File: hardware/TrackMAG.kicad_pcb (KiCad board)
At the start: 4 copper layers, 36 x 36 mm, 58 parts, among them J1 USB_C_Socket_USB2.0, J2 Conn_Debug, SW1 SW_RESET, SW2 SW_BOOT, SW3 SW_CALIBRATE, U1 LSM6DS3TR-C, U2 USBLC6-2P6, U3 STM32F103C8T6, U4 LIS2MDL, U5 AMS1117-3.3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

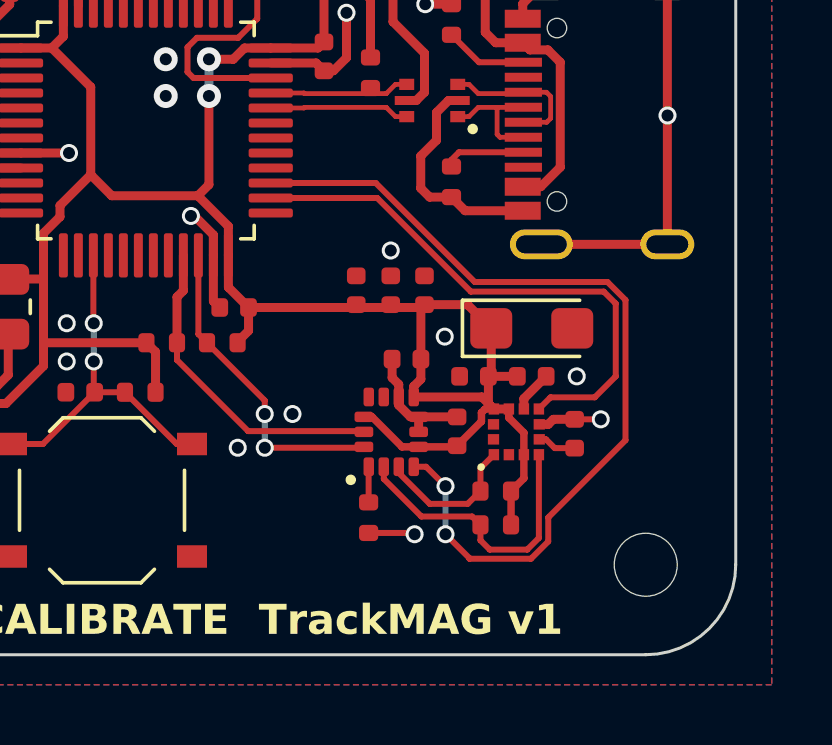
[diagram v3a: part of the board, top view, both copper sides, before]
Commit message: Increase spacing of INT1 line
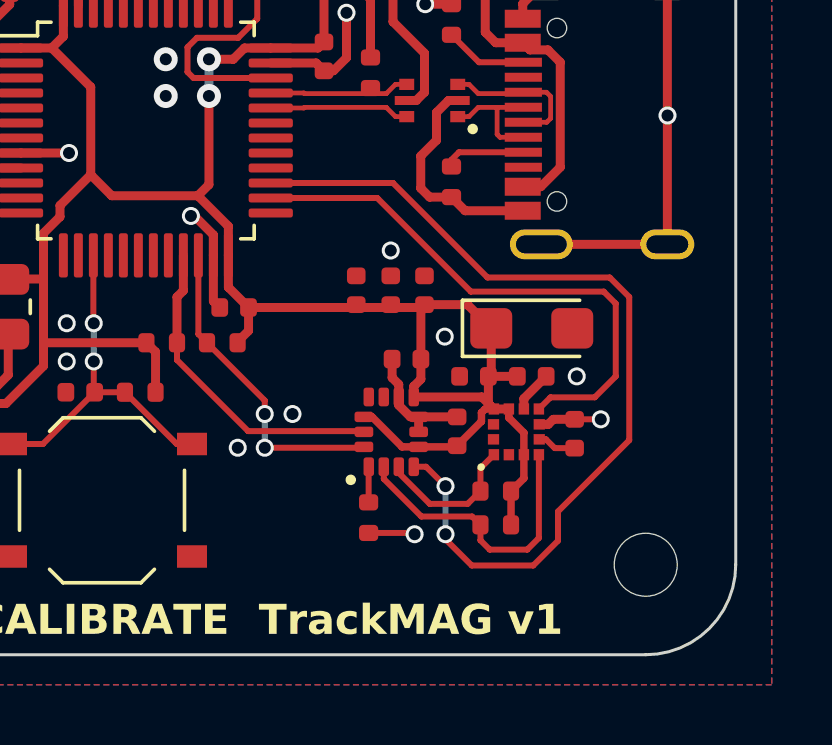
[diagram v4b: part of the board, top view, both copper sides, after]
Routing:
- net INT1: track 29.5 -> 30.2 mm
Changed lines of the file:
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@@
   (segment (start 148.6 103.495) (end 149.85 103.495) (width 0.2) (layer "F.Cu") (net 17))
   (segment (start 148.29 102.67) (end 148.29 103.185) (width 0.2) (layer "F.Cu") (net 17))
-  (segment (start 150.55 103.225) (end 150.55 102.425) (width 0.2) (layer "F.Cu") (net 18))
-  (segment (start 153.125 99.85) (end 153.125 95.175) (width 0.2) (layer "F.Cu") (net 18))
-  (segment (start 147.125 102.9825) (end 147.925 103.7825) (width 0.2) (layer "F.Cu") (net 18))
+  (segment (start 153.25 99.85) (end 153.25 95.075) (width 0.2) (layer "F.Cu") (net 18))
+  (segment (start 150.05 104.025) (end 150.875 103.2) (width 0.2) (layer "F.Cu") (net 18))
   (segment (start 146.477 100.7325) (end 147.125 101.3805) (width 0.2) (layer "F.Cu") (net 18))
-  (segment (start 153.125 95.175) (end 152.525 94.575) (width 0.2) (layer "F.Cu") (net 18))
-  (segment (start 144.8 91.275) (end 144.375 91.275) (width 0.2) (layer "F.Cu") (net 18))
-  (segment (start 141.3 91.275) (end 144.375 91.275) (width 0.2) (layer "F.Cu") (net 18))
-  (segment (start 147.925 103.8) (end 149.975 103.8) (width 0.2) (layer "F.Cu") (net 18))
-  (segment (start 147.925 103.7825) (end 147.925 103.8) (width 0.2) (layer "F.Cu") (net 18))
-  (segment (start 149.975 103.8) (end 150.55 103.225) (width 0.2) (layer "F.Cu") (net 18))
-  (segment (start 150.55 102.425) (end 153.125 99.85) (width 0.2) (layer "F.Cu") (net 18))
-  (segment (start 148.1 94.575) (end 144.8 91.275) (width 0.2) (layer "F.Cu") (net 18))
+  (segment (start 148 104.025) (end 150.05 104.025) (width 0.2) (layer "F.Cu") (net 18))
+  (segment (start 153.25 95.075) (end 152.6 94.425) (width 0.2) (layer "F.Cu") (net 18))
+  (segment (start 147.125 102.9825) (end 147.125 103.15) (width 0.2) (layer "F.Cu") (net 18))
+  (segment (start 148.525 94.425) (end 145.375 91.275) (width 0.2) (layer "F.Cu") (net 18))
+  (segment (start 152.6 94.425) (end 148.525 94.425) (width 0.2) (layer "F.Cu") (net 18))
+  (segment (start 145.375 91.275) (end 141.3 91.275) (width 0.2) (layer "F.Cu") (net 18))
+  (segment (start 147.125 103.15) (end 148 104.025) (width 0.2) (layer "F.Cu") (net 18))
   (segment (start 146.0675 100.7325) (end 146.477 100.7325) (width 0.2) (layer "F.Cu") (net 18))
-  (segment (start 152.525 94.575) (end 148.1 94.575) (width 0.2) (layer "F.Cu") (net 18))
+  (segment (start 150.875 103.2) (end 150.875 102.225) (width 0.2) (layer "F.Cu") (net 18))
   (segment (start 146.0675 100.7325) (end 146.0675 100.7375) (width 0.2) (layer "F.Cu") (net 18))
+  (segment (start 150.875 102.225) (end 153.25 99.85) (width 0.2) (layer "F.Cu") (net 18))
   (via (at 147.125 101.3805) (size 0.6) (drill 0.4) (layers "F.Cu" "B.Cu") (net 18))
   (via (at 147.125 102.9825) (size 0.6) (drill 0.4) (layers "F.Cu" "B.Cu") (net 18))

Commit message: Cleanup
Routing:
- net GND: track 72.8 -> 37.1 mm
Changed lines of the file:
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@@
   (segment (start 146.3 90.375) (end 146.3 91.45) (width 0.3) (layer "F.Cu") (net 2))
   (segment (start 130.1 90.125) (end 129.9 90.325) (width 0.3) (layer "F.Cu") (net 2))
-  (segment (start 154.52 84.68) (end 154.52 82.955) (width 0.3) (layer "F.Cu") (net 2))
-  (segment (start 127.2 87.6) (end 126.175 87.6) (width 0.2) (layer "F.Cu") (net 2))
   (segment (start 134.8875 85.3625) (end 134.8875 83.7875) (width 0.3) (layer "F.Cu") (net 2))
-  (segment (start 132.12 85.795) (end 131.175 85.795) (width 0.3) (layer "F.Cu") (net 2))
   (segment (start 150.25 99.32) (end 150.55 99.32) (width 0.3) (layer "F.Cu") (net 2))
   (segment (start 146.3 91.45) (end 146.595 91.745) (width 0.3) (layer "F.Cu") (net 2))
-  (segment (start 154.52 84.68) (end 154.52 89.02) (width 0.3) (layer "F.Cu") (net 2))
-  (segment (start 149.7 85.8) (end 149.7 85.3) (width 0.3) (layer "F.Cu") (net 2))
   (segment (start 141.3 87.275) (end 142.815 87.275) (width 0.3) (layer "F.Cu") (net 2))
-  (segment (start 150.32 93.32) (end 154.52 93.32) (width 0.3) (layer "F.Cu") (net 2))
-  (segment (start 122.69 90.375) (end 123.9 90.375) (width 0.3) (layer "F.Cu") (net 2))
   (segment (start 149.7375 98.4625) (end 149.7375 98.8075) (width 0.3) (layer "F.Cu") (net 2))
   (segment (start 139.3875 93.004523) (end 138.756292 92.373315) (width 0.3) (layer "F.Cu") (net 2))
@@
   (segment (start 125.59 88.165) (end 125.6 88.175) (width 0.2) (layer "F.Cu") (net 2))
   (segment (start 131.1 91.73) (end 130.435 91.73) (width 0.3) (layer "F.Cu") (net 2))
-  (segment (start 150.32 84.68) (end 154.52 84.68) (width 0.3) (layer "F.Cu") (net 2))
-  (segment (start 125.6 86.875) (end 125.625 86.85) (width 0.2) (layer "F.Cu") (net 2))
-  (segment (start 132.125 85.8) (end 132.12 85.795) (width 0.3) (layer "F.Cu") (net 2))
   (segment (start 129.905 90.33) (end 129.905 91.2) (width 0.3) (layer "F.Cu") (net 2))
   (segment (start 151.2625 99.32) (end 151.43 99.1525) (width 0.2) (layer "F.Cu") (net 2))
-  (segment (start 152.3 99.1525) (end 151.43 99.1525) (width 0.2) (layer "F.Cu") (net 2))
   (segment (start 146.23 99.07) (end 147.51 99.07) (width 0.3) (layer "F.Cu") (net 2))
   (segment (start 139.3875 93.6875) (end 139.3875 95.2125) (width 0.3) (layer "F.Cu") (net 2))
@@
   (segment (start 150.55 99.32) (end 150.7175 99.1525) (width 0.3) (layer "F.Cu") (net 2))
   (segment (start 150.48 97.72) (end 149.7375 98.4625) (width 0.3) (layer "F.Cu") (net 2))
-  (segment (start 149.25 81.84) (end 150.565 81.84) (width 0.3) (layer "F.Cu") (net 2))
-  (segment (start 149.7 92.2) (end 147.78 92.2) (width 0.3) (layer "F.Cu") (net 2))
   (segment (start 143.825 87.1) (end 143.825 85.6) (width 0.3) (layer "F.Cu") (net 2))
-  (segment (start 146.45 85.315) (end 147.325 85.315) (width 0.3) (layer "F.Cu") (net 2))
   (segment (start 129.9 90.325) (end 129.905 90.33) (width 0.3) (layer "F.Cu") (net 2))
-  (segment (start 125.6 88.175) (end 125.6 86.875) (width 0.3) (layer "F.Cu") (net 2))
   (segment (start 154.52 89.03) (end 154.525 89.025) (width 0.3) (layer "F.Cu") (net 2))
   (segment (start 139.3875 93.6875) (end 139.3875 93.004523) (width 0.3) (layer "F.Cu") (net 2))
-  (segment (start 132.6 84.96) (end 132.6 85.325) (width 0.3) (layer "F.Cu") (net 2))
   (segment (start 139.3875 95.2125) (end 139.6 95.425) (width 0.3) (layer "F.Cu") (net 2))
-  (segment (start 144.5625 102.94) (end 146.0525 102.94) (width 0.2) (layer "F.Cu") (net 2))
-  (segment (start 149.7 85.3) (end 150.32 84.68) (width 0.3) (layer "F.Cu") (net 2))
   (segment (start 154 78.2) (end 153.75 78.45) (width 0.3) (layer "F.Cu") (net 2))
   (segment (start 132.975 90.275) (end 131.5 90.275) (width 0.3) (layer "F.Cu") (net 2))
   (segment (start 146.3 90.375) (end 146.825 89.85) (width 0.3) (layer "F.Cu") (net 2))
-  (segment (start 154.52 82.955) (end 155.225 82.25) (width 0.3) (layer "F.Cu") (net 2))
   (segment (start 131.35 90.125) (end 130.1 90.125) (width 0.3) (layer "F.Cu") (net 2))
   (segment (start 143.075 87.535) (end 143.39 87.535) (width 0.3) (layer "F.Cu") (net 2))
   (segment (start 153.75 78.675) (end 153.75 78.45) (width 0.3) (layer "F.Cu") (net 2))
-  (segment (start 147.78 92.2) (end 147.325 91.745) (width 0.3) (layer "F.Cu") (net 2))
   (segment (start 131.5 90.275) (end 131.35 90.125) (width 0.3) (layer "F.Cu") (net 2))
-  (segment (start 132.6 85.325) (end 132.125 85.8) (width 0.3) (layer "F.Cu") (net 2))
+  (segment (start 125.675 88.1) (end 125.6 88.175) (width 0.2) (layer "F.Cu") (net 2))
   (segment (start 143.39 87.535) (end 143.825 87.1) (width 0.3) (layer "F.Cu") (net 2))
   (segment (start 134.8875 83.7875) (end 135.1 83.575) (width 0.3) (layer "F.Cu") (net 2))
   (segment (start 147.51 99.07) (end 147.5125 99.0725) (width 0.3) (layer "F.Cu") (net 2))
   (segment (start 145.5675 98.4075) (end 145.5675 98.683155) (width 0.3) (layer "F.Cu") (net 2))
-  (segment (start 135.1 83.575) (end 136.15 83.575) (width 0.3) (layer "F.Cu") (net 2))
   (segment (start 146.825 89.85) (end 146.825 88.925) (width 0.3) (layer "F.Cu") (net 2))
   (segment (start 154.52 89.02) (end 154.525 89.025) (width 0.3) (layer "F.Cu") (net 2))
-  (segment (start 154.52 93.32) (end 154.52 89.03) (width 0.3) (layer "F.Cu") (net 2))
   (segment (start 146.0525 102.94) (end 146.095 102.9825) (width 0.2) (layer "F.Cu") (net 2))
-  (segment (start 130.225 85.795) (end 131.175 85.795) (width 0.3) (layer "F.Cu") (net 2))
   (segment (start 145.5675 98.4075) (end 145.5675 97.9875) (width 0.3) (layer "F.Cu") (net 2))
   (segment (start 145.954345 99.07) (end 146.23 99.07) (width 0.3) (layer "F.Cu") (net 2))
@@
   (via (at 137.8 87.15) (size 0.8) (drill 0.4) (layers "F.Cu" "B.Cu") (free) (net 2))
   (via (at 154.525 89.025) (size 0.6) (drill 0.4) (layers "F.Cu" "B.Cu") (net 2))
-  (via (at 125.625 86.85) (size 0.6) (drill 0.4) (layers "F.Cu" "B.Cu") (net 2))
+  (via (at 125.675 86.85) (size 0.6) (drill 0.4) (layers "F.Cu" "B.Cu") (net 2))
   (via (at 136.15 83.575) (size 0.6) (drill 0.4) (layers "F.Cu" "B.Cu") (net 2))
   (via (at 130.225 85.795) (size 0.6) (drill 0.4) (layers "F.Cu" "B.Cu") (net 2))

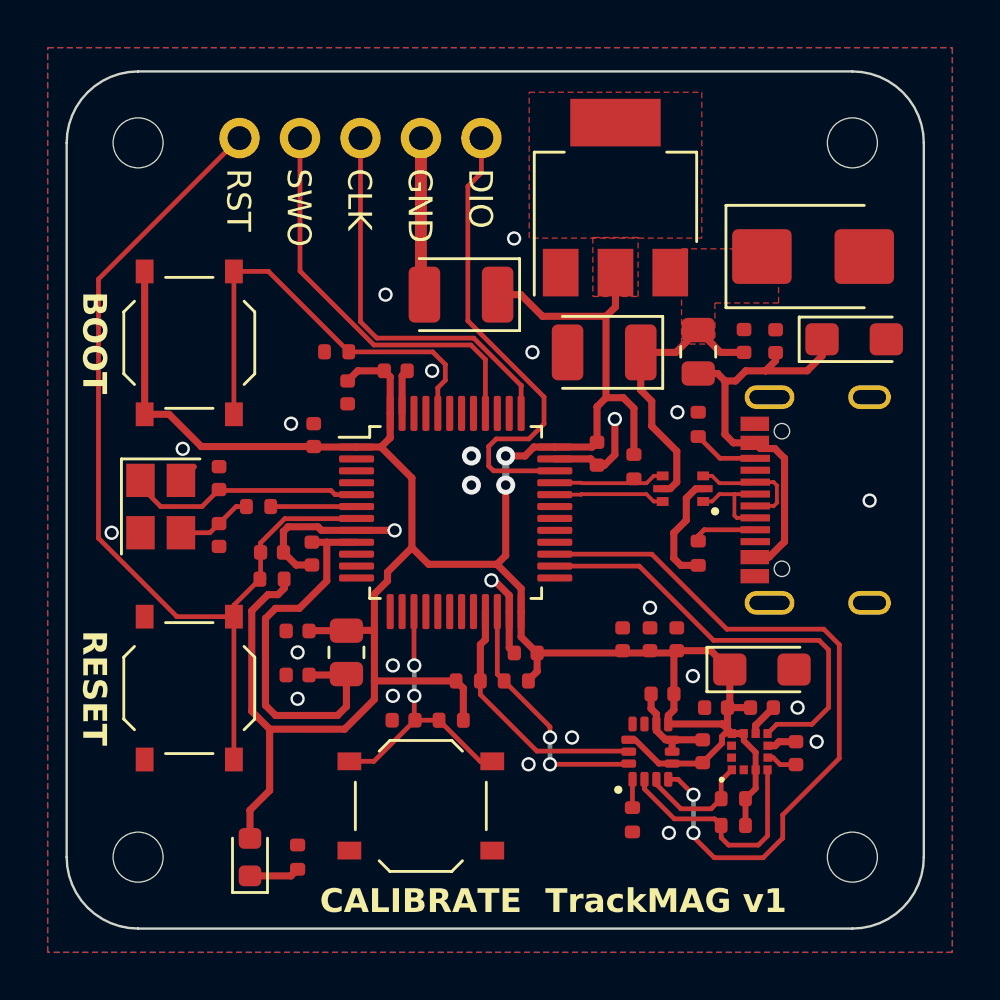
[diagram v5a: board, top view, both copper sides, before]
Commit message: Remove UART pin header from position files
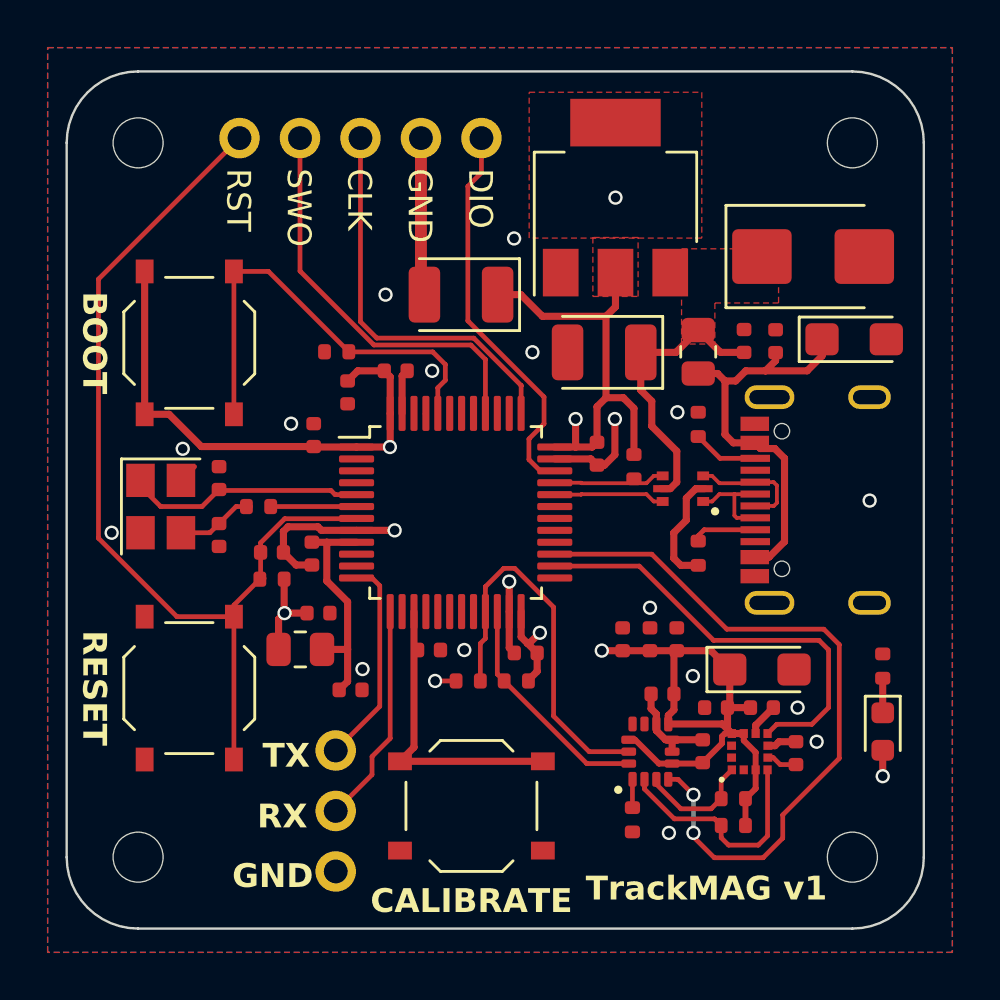
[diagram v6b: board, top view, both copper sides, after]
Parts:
- removed the R12 at (136.9, 98.2)
- added J2: UART, TrackMAG:PinHeader_1x03_P2.54mm_UART, F.Cu at (132.1, 104.6)
- J3: renamed from J2; value Conn_Debug -> Debug
- moved D1 27.1 mm to (155.1, 98.7), turned to -90 degrees
- moved R12 25.9 mm to (155.1, 96.0)
- moved C23 3.14 mm to (136.0, 95.3), turned to 0 degrees
- moved C15 2.31 mm to (132.7, 97.0), turned to 0 degrees
- moved SW3 2.12 mm to (137.8, 101.8)
- moved FB1 1.94 mm to (130.6, 95.3), turned to 180 degrees
- moved C16 1.15 mm to (131.4, 93.8), turned to 0 degrees
- renumbered R13 to R12
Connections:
- U3 pad 12: unconnected-(U3-PA2-Pad12) -> /TX
- U3 pad 13: unconnected-(U3-PA3-Pad13) -> /RX
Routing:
- net +3.3V: track 121.9 -> 77.1 mm, vias 2 -> 8
- net /RX: track 0.00 -> 9.32 mm
- net /TX: track 0.00 -> 8.80 mm
- net +3.3VA: track 16.9 -> 9.51 mm
- net I2C2_SCL: track 10.8 -> 16.3 mm
- net /SWDIO: track 20.2 -> 16.9 mm
- net I2C2_SDA: track 10.7 -> 9.74 mm, vias 2 -> 0
- net Net-(D1-K): track 2.11 -> 1.45 mm
- net CALIBRATE: track 12.0 -> 12.5 mm, vias 2 -> 0
- net GND: track 37.1 -> 36.6 mm, vias 25 -> 19
- added copper zone on In2.Cu, net +3.3V
- removed copper zone on In2.Cu, net GND
